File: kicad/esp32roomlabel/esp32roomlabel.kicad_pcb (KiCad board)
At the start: 2 copper layers, 94 x 53.3 mm, 11 parts, among them J1 BME280, J2 OLED, J3 LCD2004, J4 DS3231, J5 DHT22, J6 Switch1, J7 Switch2, J8 MISC, J9 LED, U1 NODEMCU ESP32

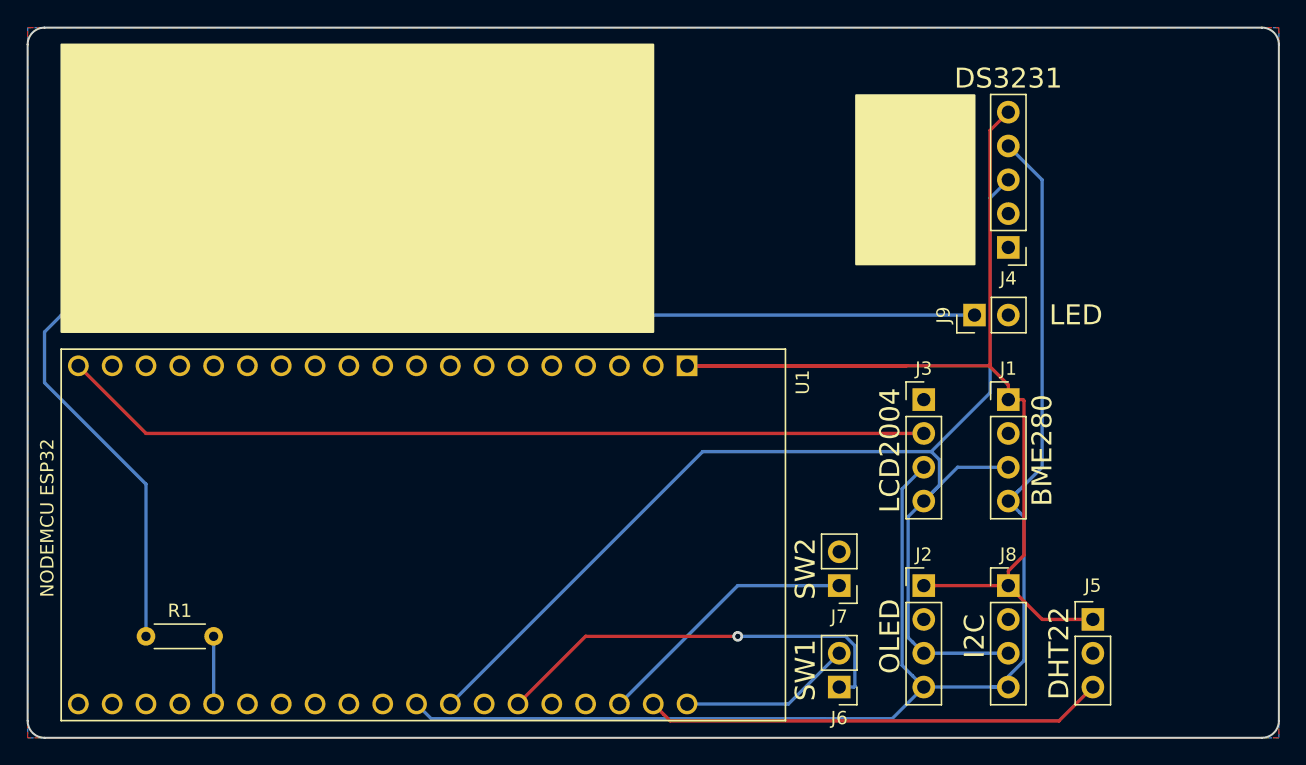
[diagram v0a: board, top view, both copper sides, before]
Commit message: Updated PCB
Added GPIO and Analog pin header
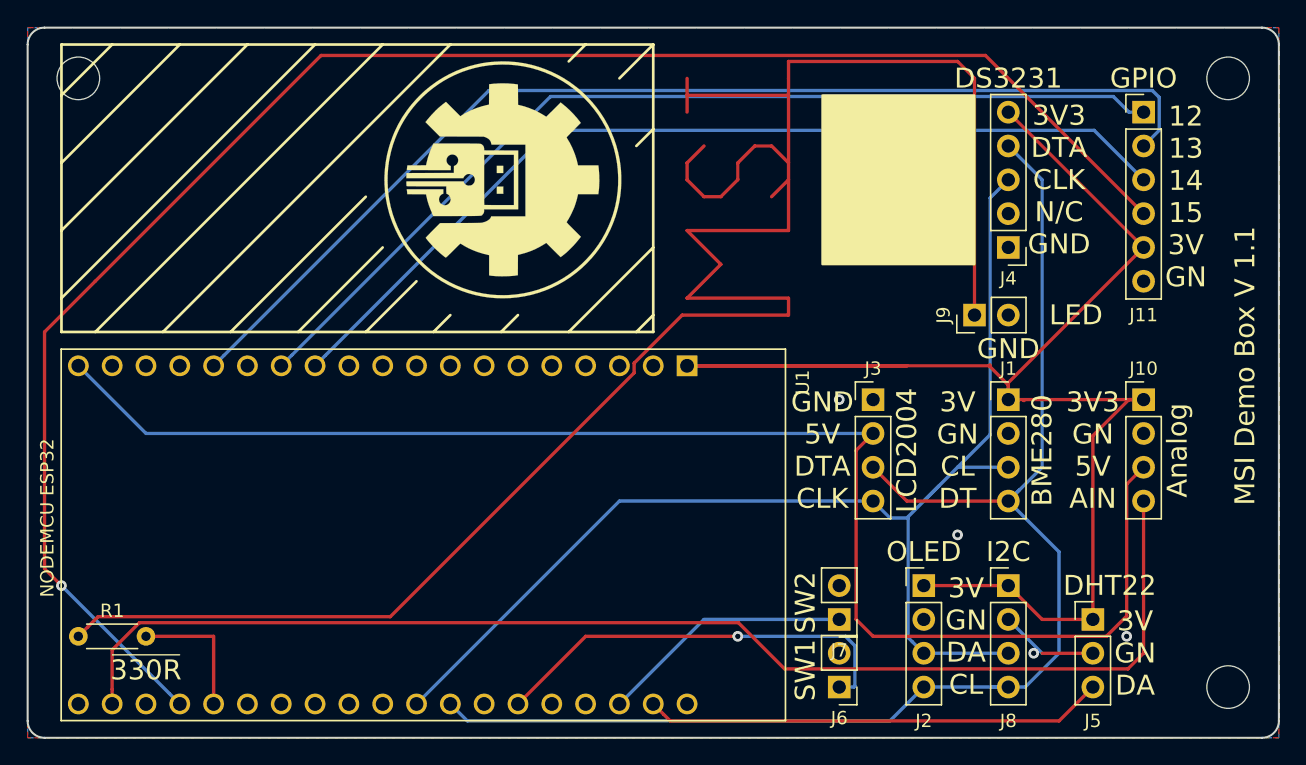
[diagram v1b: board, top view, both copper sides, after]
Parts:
- added ?: MountingHole_3.2mm_M3_DIN965, MountingHole:MountingHole_3.2mm_M3_DIN965, F.Cu at (152.4, 125.7)
- added ?: MountingHole_3.2mm_M3_DIN965, MountingHole:MountingHole_3.2mm_M3_DIN965, F.Cu at (152.4, 80.0)
- added ?: MountingHole_3.2mm_M3_DIN965, MountingHole:MountingHole_3.2mm_M3_DIN965, F.Cu at (66.0, 80.0)
- added ?: , ESP32-DEVKIT:LOGO, F.Cu at (97.8, 87.6)
- added J10: Analog, Connector_PinHeader_2.54mm:PinHeader_1x04_P2.54mm_Vertical, F.Cu at (146.1, 104.1)
- added J11: GPIO, Connector_PinHeader_2.54mm:PinHeader_1x06_P2.54mm_Vertical, F.Cu at (146.1, 82.5)
- J8: value MISC -> I2C
- moved R1 5.08 mm to (66.0, 121.9)
- moved J3 3.81 mm to (125.7, 104.1)
- moved J7 2.54 mm to (123.2, 120.7)
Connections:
- U1 pad 12: Net-(U1-Pad12) -> GPIO14
- U1 pad 13: Net-(U1-Pad13) -> GPIO12
- U1 pad 15: Net-(U1-Pad15) -> GPIO13
- U1 pad 27: CLK -> DTA
- U1 pad 28: DTA -> CLK
- U1 pad 35: Net-(U1-Pad35) -> GPIO15
- U1 pad 37: Net-(U1-Pad37) -> AnalogIn
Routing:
- net GPIO15: track 0.00 -> 128.0 mm, vias 0 -> 1
- net AnalogIn: track 0.00 -> 95.7 mm
- net GPIO13: track 0.00 -> 83.9 mm
- net GPIO12: track 0.00 -> 73.6 mm
- net GPIO14: track 0.00 -> 71.1 mm
- net Net-(J9-Pad1): track 96.4 -> 158.4 mm
- net 5V: track 65.6 -> 109.5 mm
- net 3V3: track 91.3 -> 115.2 mm
- net DTA: track 109.6 -> 103.0 mm
- net GND: track 13.0 -> 7.40 mm, vias 0 -> 4
- net Net-(R1-Pad2): track 5.08 -> 10.2 mm
- net CLK: track 97.4 -> 94.7 mm
- net SW2: track 20.2 -> 19.1 mm
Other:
- board text added: "12 13 14 15 3V GN"
- board text added: "3V GN CL DT"
- board text added: "3V GN DA"
- board text added: "3V GN DA CL"
- board text added: "3V3 DTA CLK N/C GND"
- board text added: "3V3 GN 5V AIN"
- board text added: "Analog"
- board text added: "GND"
- board text added: "GND 5V DTA CLK"
- board text added: "GPIO"
- board text added: "MSI Demo Box V 1.1"
- board text added: "~330R"
